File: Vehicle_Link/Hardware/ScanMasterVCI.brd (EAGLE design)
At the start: 65 x 39.4 mm, 88 parts, among them IC1 XMEGA32A4U, IC2 TL331, Q1 RUM002N05, Q10 ZXMP6A17G, Q3 RUM002N05, Q4 RUM002N05, Q5 RRF015P03, Q6 RUM002N05, Q7 RRF015P03, Q8 RRF015P03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

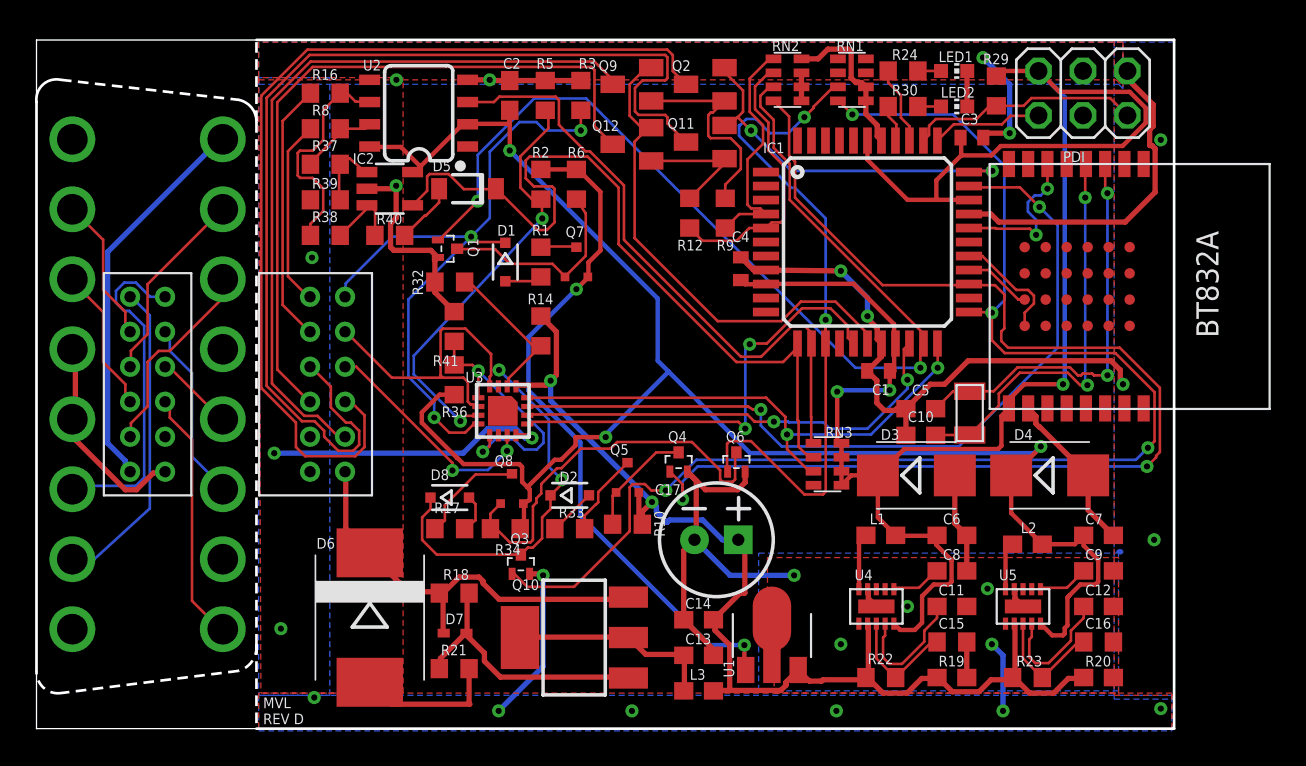
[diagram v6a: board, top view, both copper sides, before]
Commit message: Switched XMEGA to the 44QFN variety. Changed the OBD connection, expanded the size of the board just a little to accomodate the new connector.
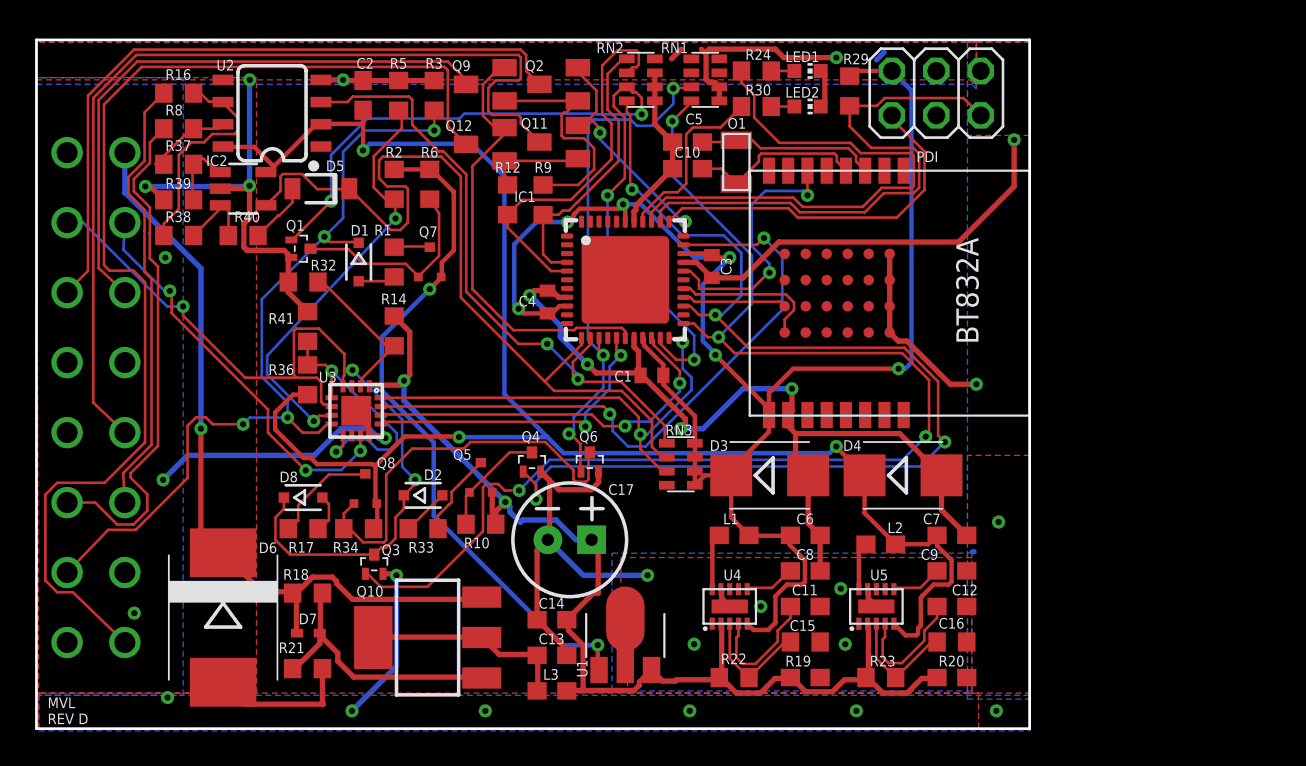
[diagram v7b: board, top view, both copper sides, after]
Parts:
- removed C18: J1962M, customics:J1962M
- removed U$1: DF11-12DP-2DS, customics:DF11-12DP-2DS
- removed U$2: DF11-12DS-2DS, customics:DF11-12DS-2DSA
- added OBD1: (no value), customics:OBD2
- IC1: device atmel:TQFP44 -> atmel:MLF44-TH
- moved C10 20.3 mm to (37.2, 32.0)
- moved C5 20.3 mm to (37.2, 33.5)
- moved O1 19.6 mm to (40.0, 32.4)
- moved C3 16.6 mm to (38.6, 26.4), turned to 270 degrees
- moved IC1 14.0 mm to (33.7, 25.7)
- moved U6 13.7 mm to (48.8, 24.9)
- moved C1 13.0 mm to (35.2, 20.2)
- moved C4 11.2 mm to (29.2, 24.4)
- moved R12 10.4 mm to (26.9, 30.2)
- moved R9 10.4 mm to (29.0, 30.2)
- moved C12 8.38 mm to (52.3, 6.99)
- moved C16 8.38 mm to (52.3, 2.92)
- moved C7 8.38 mm to (52.3, 11.0)
- moved C9 8.38 mm to (52.3, 9.02)
- moved D3 8.38 mm to (41.9, 14.5)
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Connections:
- removed net CGND: C18.4, C18.5, U$2.P$12
- removed net CVBATT: C18.16, U$2.P$6
- removed net N$25: C18.15, U$2.P$3
- removed net N$28: C18.14, U$2.P$5
- removed net N$29: C18.6, U$2.P$4
- removed net N$32: C18.7, U$2.P$2
- removed net N$41: C18.3, U$2.P$7
- removed net N$42: C18.9, U$2.P$10
- removed net N$43: C18.12, U$2.P$9
- removed net N$44: C18.11, U$2.P$8
- removed net N$46: C18.2, U$2.P$1
- net GND: now also OBD1.4, OBD1.5, U3.PAD; no longer U$1.P$12
- net J1962-11: now also OBD1.11; no longer U$1.P$8
- net J1962-12: now also OBD1.12; no longer U$1.P$9
- net J1962-14: now also OBD1.14; no longer U$1.P$5
- net J1962-15: now also OBD1.15; no longer U$1.P$3
- net J1962-16: now also OBD1.16; no longer U$1.P$6
- net J1962-2: now also OBD1.2; no longer U$1.P$1
- net J1962-3: now also OBD1.3; no longer U$1.P$7
- net J1962-6: now also OBD1.6; no longer U$1.P$4
- net J1962-7: now also OBD1.7; no longer U$1.P$2
- net J1962-9: now also OBD1.9; no longer U$1.P$10
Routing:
- net GND: track 173.8 -> 203.5 mm, vias 26 -> 28
- net PWR-LED: track 4.48 -> 31.3 mm
- net J1962-9: track 41.6 -> 64.2 mm
- net CVBATT: track 22.3 -> 0.00 mm
- net J1962-16: track 24.4 -> 44.4 mm, vias 0 -> 1
- net N$41: track 19.2 -> 0.00 mm
- net J1962-3: track 10.7 -> 29.6 mm
- net PDI_CLK: track 13.4 -> 32.2 mm
- net N$46: track 18.2 -> 0.00 mm
- net J1962-6: track 55.7 -> 40.1 mm
- net PDI_DATA: track 6.37 -> 20.8 mm
- net N$42: track 14.4 -> 0.00 mm
- net N$24: track 23.6 -> 10.1 mm, vias 2 -> 0
- net N$13: track 23.2 -> 10.3 mm, vias 2 -> 0
- net CGND: track 12.2 -> 0.00 mm
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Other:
- board size 65 x 39.4 mm -> 56.8 x 39.4 mm

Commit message: Switched voltage ICs to new 600mA chips for easier soldering. Board layout still WIP. Switched XMEGA to be no-lead to save space
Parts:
- removed C15, C16: 2.2uF, adafruit:C0603
- removed R19, R20: 866k, adafruit:R0603
- removed R22, R23: 3.32M, adafruit:R0603
- C11: value 1uF -> 10uF; device adafruit:C0603 -> SparkFun-Capacitors:0603
- C12: value 1uF -> 0.1uF; device adafruit:C0603 -> SparkFun-Capacitors:0603
- C6, C7: value 22uF -> 2.2uF; device adafruit:C0603 -> SparkFun-Capacitors:1206
- C8: value 3.3nF -> 0.1uF; device adafruit:C0603 -> SparkFun-Capacitors:0603
- C9: value 3.3nF -> 10uF; device adafruit:C0603 -> SparkFun-Capacitors:0603
- D3: value SMBJ3V3HE3 -> SM5817PL; device diode:SMB -> customics:SOD123FL
- D4: value SMAJ5.0A -> SM5817PL; device diode:SMB -> customics:SOD123FL
- L1: value 22uH -> (none); device customics:L0603 -> inductor-neosid:SM-1206
- L2: value 15uH -> (none); device customics:L0603 -> inductor-neosid:SM-1206
- U4: value MAX17502EATB+ -> LMR16006YQ5; device customics:TDFN-10-EP -> customics:SOT6
- U5: value MAX17502FATB+ -> LMR16006YQ3; device customics:TDFN-10-EP -> customics:SOT6
- moved U4 12.5 mm to (51.9, 4.70), turned to 270 degrees
- moved L1 11.9 mm to (51.8, 11.2), turned to 180 degrees
- moved D3 11.7 mm to (51.4, 7.75), turned to 180 degrees
- moved C12 10.1 mm to (42.3, 6.22), turned to 270 degrees
- moved C8 8.64 mm to (52.6, 9.40)
- moved C6 8.18 mm to (37.3, 6.22), turned to 90 degrees
- moved U5 8.04 mm to (40.0, 6.22), turned to 270 degrees
- moved D4 8.00 mm to (42.0, 11.7)
- moved C11 7.89 mm to (41.9, 14.6)
- moved C7 7.68 mm to (46.4, 6.22), turned to 90 degrees
- moved C9 6.69 mm to (48.6, 14.6)
- moved L2 6.02 mm to (44.1, 6.22), turned to 90 degrees
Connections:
- removed net N$15: C12.1, U5.4
- removed net N$16: R20.2, R23.1, U5.3
- removed net N$17: C9.1, U5.6
- removed net N$19: L2.1, U5.10
- net +12V: now also C6.1, C7.1, U4.4, U4.5, U5.4, U5.5; no longer C15.1, C16.1, R22.2, R23.2, U4.2, U5.2
- net +3V3: now also C11.1, L2.2, U5.3; no longer C6.1, D3.C, L1.2, U4.5
- net +5V: now also C9.1, L1.2, U4.3; no longer C7.1, D4.C, L2.2, U5.5
- net GND: now also U4.2, U5.2; no longer C12.2, C15.2, C16.2, C8.2, R19.1, R20.1, U4.1, U4.9, U4.EPAD, U5.1, U5.9, U5.EPAD
- net N$12: now also C12.1, U5.1; no longer L1.1, U4.10
- net N$3: now also U4.1; no longer U4.6
- net N$7: now also C8.2, D3.C, L1.1, U4.6; no longer R19.2, R22.1, U4.3
- net N$9: now also C12.2, D4.C, L2.1, U5.6; no longer C11.1, U4.4
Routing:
- net +12V: track 66.0 -> 44.9 mm
- net +5V: track 98.0 -> 79.5 mm
- net GND: track 203.5 -> 186.9 mm
- net +3V3: track 97.6 -> 82.5 mm
- net N$9: track 7.33 -> 0.00 mm
- net N$15: track 7.29 -> 0.00 mm
- net N$7: track 6.74 -> 0.00 mm
- net N$16: track 6.74 -> 0.00 mm
- net N$12: track 3.24 -> 0.00 mm
- net N$3: track 2.92 -> 0.00 mm
- net N$17: track 2.91 -> 0.00 mm
- net N$19: track 2.74 -> 0.00 mm
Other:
- board text added: "MVL REV E"
- board text removed: "MVL REV D"
